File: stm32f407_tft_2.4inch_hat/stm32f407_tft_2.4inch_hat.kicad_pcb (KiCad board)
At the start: 2 copper layers, 62.5 x 71 mm, 3 parts, among them P1 Conn_02x25_Row_Letter_First_S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, P2 Conn_02x25_Row_Letter_First_S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, U1 CR2013-MI2120

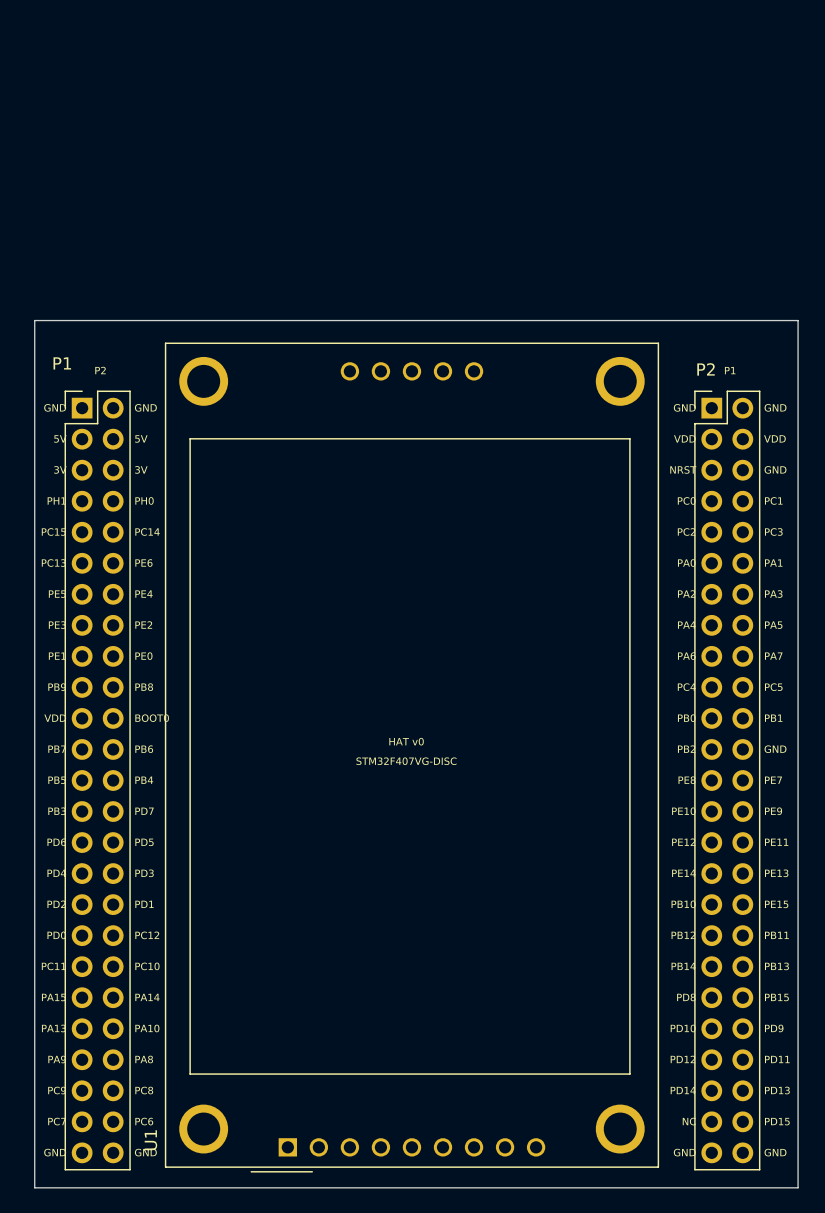
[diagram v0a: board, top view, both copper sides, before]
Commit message: Add 3 connector for i2c & uart
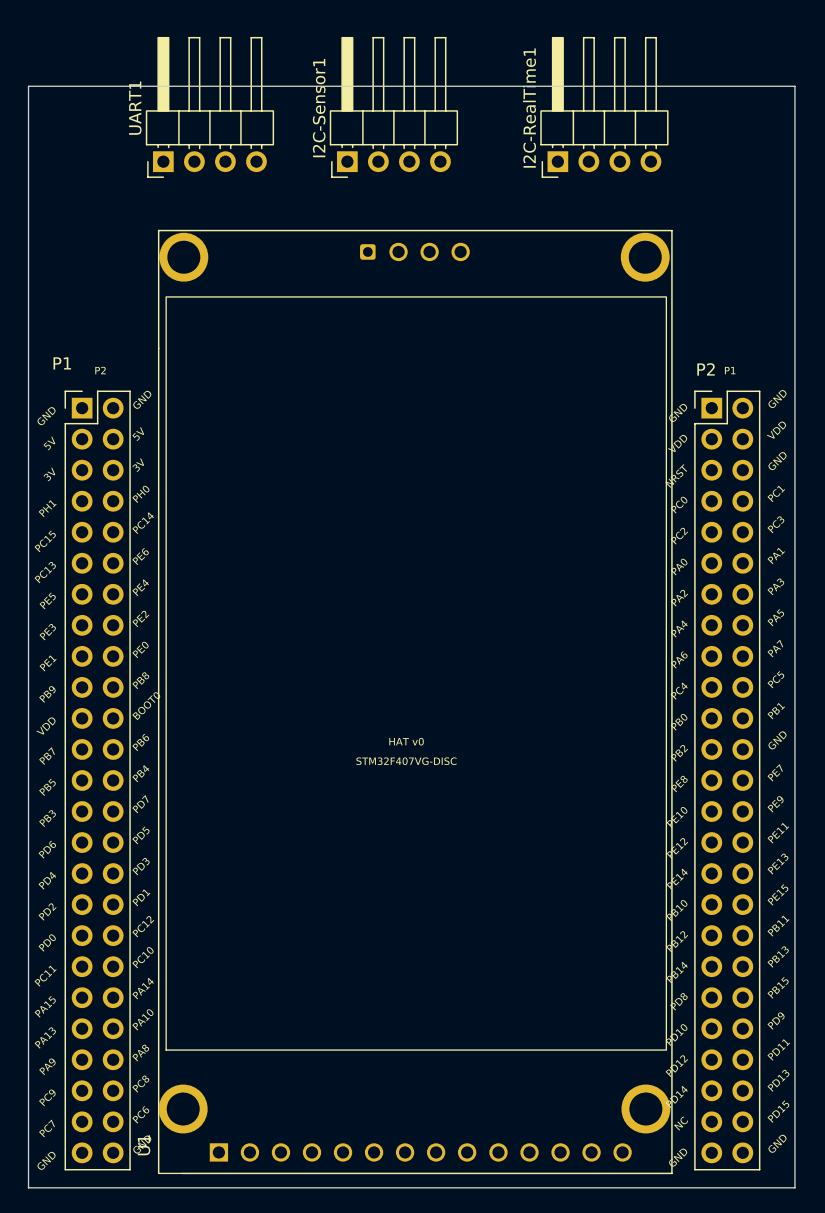
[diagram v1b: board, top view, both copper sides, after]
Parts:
- added I2C-RealTime1: Conn_01x04_Pin, Connector_PinHeader_2.54mm:PinHeader_1x04_P2.54mm_Horizontal, F.Cu at (160.2, 50.8)
- added I2C-Sensor1: Conn_01x04_Pin, Connector_PinHeader_2.54mm:PinHeader_1x04_P2.54mm_Horizontal, F.Cu at (142.9, 50.8)
- added UART1: Conn_01x04_Pin, Connector_PinHeader_2.54mm:PinHeader_1x04_P2.54mm_Horizontal, F.Cu at (127.9, 50.8)
- P1: value Conn_02x25_Row_Letter_First_Shielded -> STM32F407-DISC P1
- P2: value Conn_02x25_Row_Letter_First_Shielded -> STM32F407-DISC P2
- U1: value CR2013-MI2120 -> TFT SPI 240x320
- moved U1 0.70 mm to (137.5, 131.9)
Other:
- board size 62.5 x 71 mm -> 62.7 x 90.2 mm

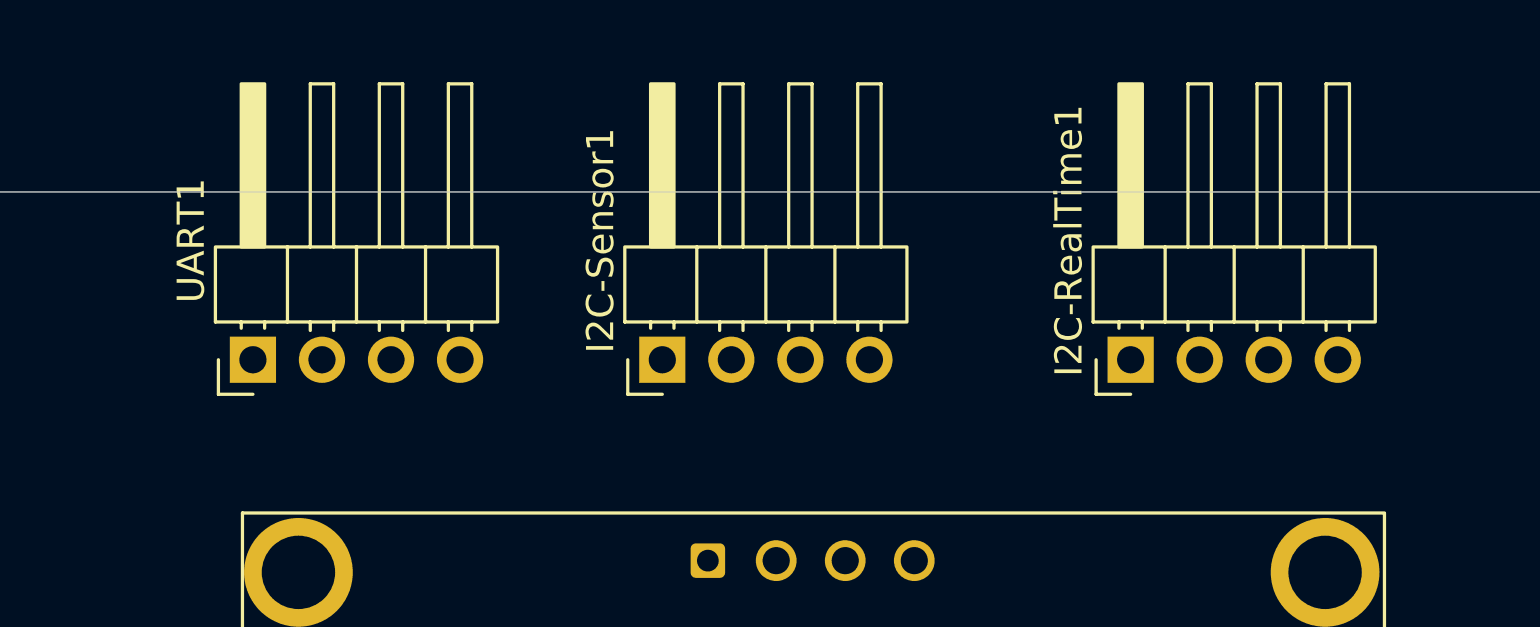
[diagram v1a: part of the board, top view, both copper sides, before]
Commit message: Update sch pin j1 & j2
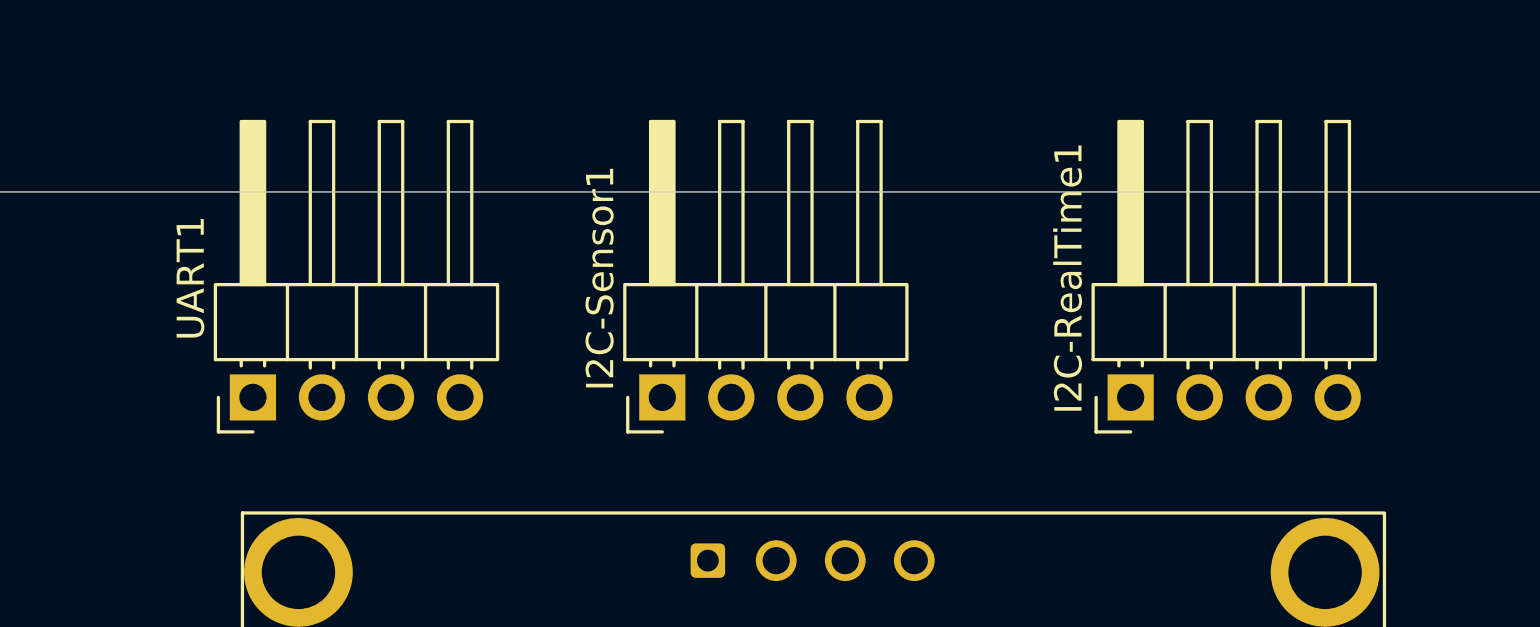
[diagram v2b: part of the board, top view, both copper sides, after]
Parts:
- moved I2C-RealTime1 1.38 mm to (160.2, 52.1)
- moved I2C-Sensor1 1.38 mm to (142.9, 52.1)
- moved UART1 1.38 mm to (127.9, 52.1)
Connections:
- I2C-RealTime1 pad 1: unconnected-(I2C-RealTime1-Pin_1-Pad1) -> /I2C_SDA
- I2C-RealTime1 pad 2: unconnected-(I2C-RealTime1-Pin_2-Pad2) -> /3V
- I2C-RealTime1 pad 3: unconnected-(I2C-RealTime1-Pin_3-Pad3) -> /GND
- I2C-RealTime1 pad 4: unconnected-(I2C-RealTime1-Pin_4-Pad4) -> /I2C_SCL
- I2C-Sensor1 pad 1: unconnected-(I2C-Sensor1-Pin_1-Pad1) -> /I2C_SDA
- I2C-Sensor1 pad 2: unconnected-(I2C-Sensor1-Pin_2-Pad2) -> /3V
- I2C-Sensor1 pad 3: unconnected-(I2C-Sensor1-Pin_3-Pad3) -> /GND
- I2C-Sensor1 pad 4: unconnected-(I2C-Sensor1-Pin_4-Pad4) -> /I2C_SCL
- P1 pad 1: (no net) -> /GND
- P1 pad 10: (no net) -> /PA9
- P1 pad 11: (no net) -> /PA14
- P1 pad 12: (no net) -> /PA13
- P1 pad 13: (no net) -> /PC10
- P1 pad 14: (no net) -> /PA15
- P1 pad 15: (no net) -> /PC12
- P1 pad 16: (no net) -> /PC11
- P1 pad 17: (no net) -> /PD1
- P1 pad 18: (no net) -> /PD0
- P1 pad 19: (no net) -> /PD3
- P1 pad 2: (no net) -> /GND
- P1 pad 20: (no net) -> /PD2
- P1 pad 21: (no net) -> /PD5
- P1 pad 22: (no net) -> /PD4
- P1 pad 23: (no net) -> /PD7
- P1 pad 24: (no net) -> /PD6
- P1 pad 25: (no net) -> /PB4
- P1 pad 26: (no net) -> /PB3
- P1 pad 27: (no net) -> /PB6
- P1 pad 28: (no net) -> /PB5
- P1 pad 29: (no net) -> /BOOT0
- P1 pad 3: (no net) -> /PC6
- P1 pad 30: (no net) -> /PB7
- P1 pad 31: (no net) -> /PB8
- P1 pad 32: (no net) -> /GND
- P1 pad 33: (no net) -> /PE0
- P1 pad 34: (no net) -> /PB9
- P1 pad 35: (no net) -> /PE2
- P1 pad 36: (no net) -> /PE1
- P1 pad 37: (no net) -> /PE4
- P1 pad 38: (no net) -> /PE3
- P1 pad 39: (no net) -> /PE6
- P1 pad 4: (no net) -> /GND
- P1 pad 40: (no net) -> /PE5
- P1 pad 41: (no net) -> /PC14
- P1 pad 42: (no net) -> /PC15
- P1 pad 43: (no net) -> /PH0
- P1 pad 44: (no net) -> /PH1
- P1 pad 45: (no net) -> /3V
- P1 pad 46: (no net) -> /3V
- P1 pad 47: (no net) -> /5V
- P1 pad 48: (no net) -> /5V
- P1 pad 49: (no net) -> /GND
- P1 pad 5: (no net) -> /PC8
- P1 pad 50: (no net) -> /GND
- P1 pad 6: (no net) -> /PC7
- P1 pad 7: (no net) -> /PA8
- P1 pad 8: (no net) -> /PC9
- P1 pad 9: (no net) -> /PA10
- P2 pad 1: (no net) -> /GND
- P2 pad 10: (no net) -> /PD9
- P2 pad 11: (no net) -> /PD8
- P2 pad 12: (no net) -> /PB15
- P2 pad 13: (no net) -> /PB14
- P2 pad 14: (no net) -> /PB13
- P2 pad 15: (no net) -> /PB12
- P2 pad 16: (no net) -> unconnected-(P2-PA5-Pad16)
- P2 pad 17: (no net) -> /PB10
- P2 pad 18: (no net) -> /PE15
- P2 pad 19: (no net) -> /PE14
- P2 pad 2: (no net) -> /GND
- P2 pad 20: (no net) -> /PE13
- P2 pad 21: (no net) -> /PE12
- P2 pad 22: (no net) -> /PE11
- P2 pad 23: (no net) -> /PE10
- P2 pad 24: (no net) -> /PE9
- P2 pad 25: (no net) -> /PE8
- P2 pad 26: (no net) -> /PE7
- P2 pad 27: (no net) -> /PB2
- P2 pad 28: (no net) -> /GND
- P2 pad 29: (no net) -> /PB0
- P2 pad 3: (no net) -> /NC
- P2 pad 30: (no net) -> /PB1
- P2 pad 31: (no net) -> /PC4
- P2 pad 32: (no net) -> /PC5
- P2 pad 33: (no net) -> /PA6
- P2 pad 34: (no net) -> /PA7
- P2 pad 35: (no net) -> /PA4
- P2 pad 36: (no net) -> /PA5
- P2 pad 37: (no net) -> unconnected-(P2-PB14-Pad37)
- P2 pad 38: (no net) -> /PA3
- P2 pad 39: (no net) -> /PA0
- P2 pad 4: (no net) -> /PD15
- P2 pad 40: (no net) -> /PA1
- P2 pad 41: (no net) -> /GND
- P2 pad 42: (no net) -> /PC3
- P2 pad 43: (no net) -> /GND
- P2 pad 44: (no net) -> /PC1
- P2 pad 45: (no net) -> /GND
- P2 pad 46: (no net) -> /GND
- P2 pad 47: (no net) -> /GND
- P2 pad 48: (no net) -> /GND
- P2 pad 49: (no net) -> /GND
- P2 pad 5: (no net) -> /PD14
- P2 pad 50: (no net) -> /GND
- P2 pad 6: (no net) -> /PD13
- P2 pad 7: (no net) -> /PD12
- P2 pad 8: (no net) -> /PD11
- P2 pad 9: (no net) -> /PD10
- UART1 pad 1: unconnected-(UART1-Pin_1-Pad1) -> /3V
- UART1 pad 2: unconnected-(UART1-Pin_2-Pad2) -> /UART_RX
- UART1 pad 3: unconnected-(UART1-Pin_3-Pad3) -> /UART_TX
- UART1 pad 4: unconnected-(UART1-Pin_4-Pad4) -> /GND

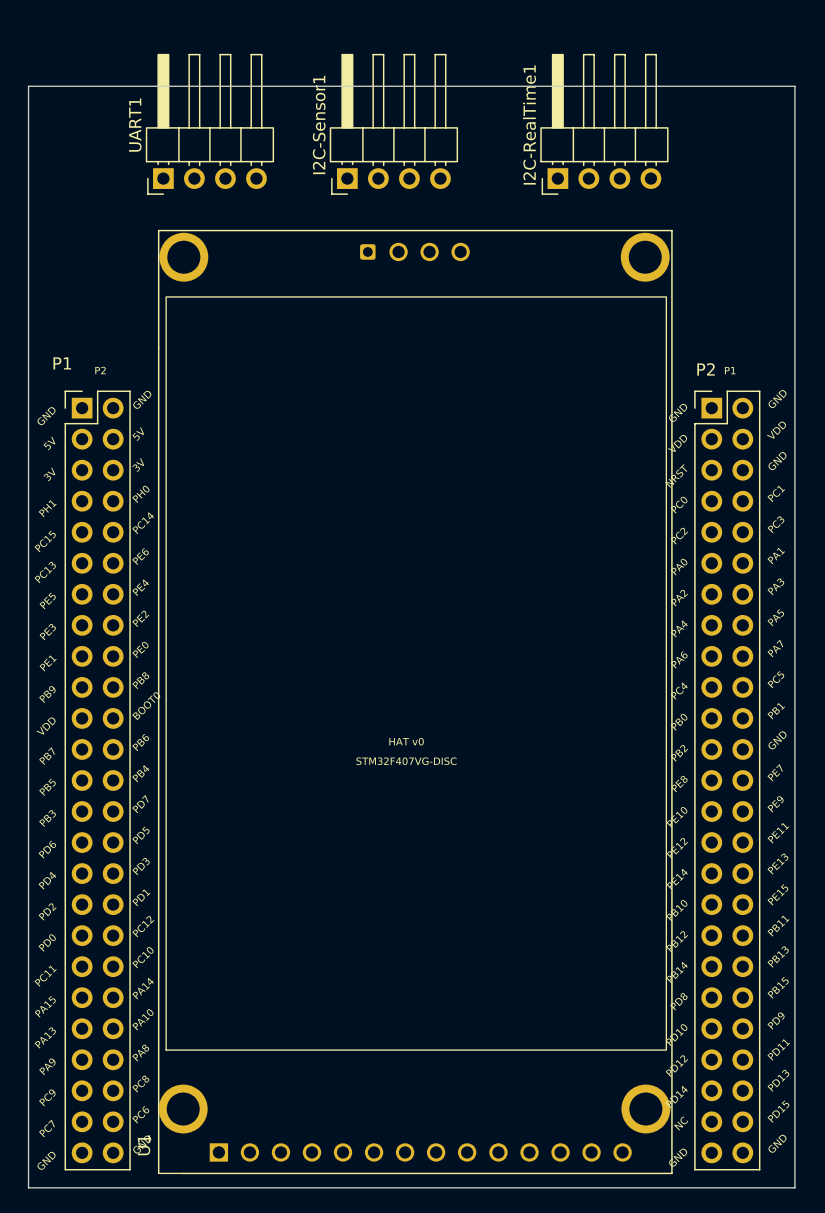
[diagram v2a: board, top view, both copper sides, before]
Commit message: Fix pinout pcb & sch are not correct
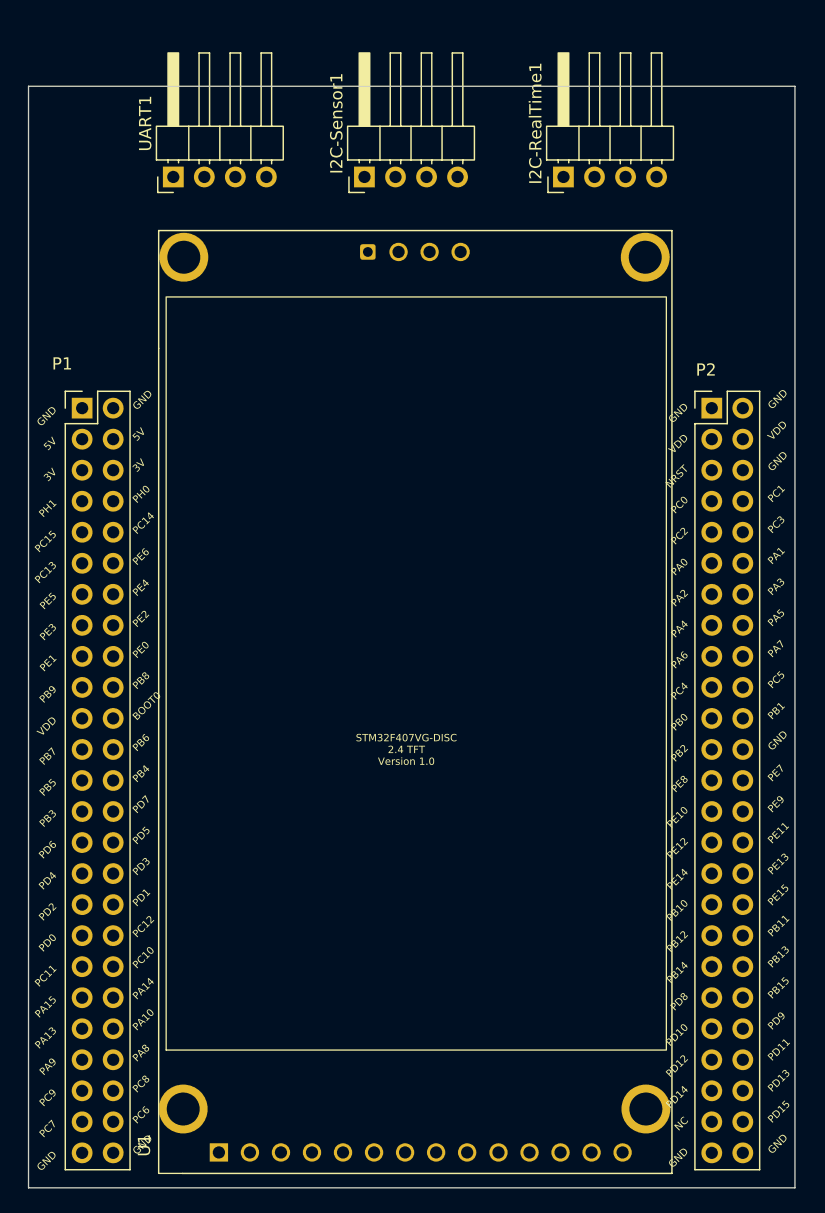
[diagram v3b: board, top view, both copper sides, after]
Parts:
- moved I2C-Sensor1 1.41 mm to (144.3, 52.0)
- moved UART1 0.82 mm to (128.7, 52.0)
- moved I2C-RealTime1 0.48 mm to (160.6, 52.0)
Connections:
- I2C-RealTime1 pad 1: /I2C_SDA -> /I2C2_SCL
- I2C-RealTime1 pad 2: /3V -> /I2C2_SDA
- I2C-RealTime1 pad 3: /GND -> /3V
- I2C-RealTime1 pad 4: /I2C_SCL -> /GND
- I2C-Sensor1 pad 1: /I2C_SDA -> /I2C2_SCL
- I2C-Sensor1 pad 2: /3V -> /I2C2_SDA
- I2C-Sensor1 pad 3: /GND -> /3V
- I2C-Sensor1 pad 4: /I2C_SCL -> /GND
- P1 pad 10: /PA9 -> /PC14
- P1 pad 11: /PA14 -> /LCD_T_IRQ
- P1 pad 12: /PA13 -> /PE6
- P1 pad 13: /PC10 -> /LCD_T_CS
- P1 pad 14: /PA15 -> /LCD_SD_CS
- P1 pad 15: /PC12 -> /PE1
- P1 pad 16: /PC11 -> /PE2
- P1 pad 17: /PD1 -> /LCD_CS
- P1 pad 18: /PD0 -> /PE0
- P1 pad 19: /PD3 -> /VDD
- P1 pad 20: /PD2 -> /PB8
- P1 pad 21: /PD5 -> /PB7
- P1 pad 22: /PD4 -> /BOOT0
- P1 pad 23: /PD7 -> /PB5
- P1 pad 24: /PD6 -> /PB6
- P1 pad 25: /PB4 -> /PB3
- P1 pad 26: /PB3 -> /PB4
- P1 pad 27: /PB6 -> /PD6
- P1 pad 28: /PB5 -> /PD7
- P1 pad 29: /BOOT0 -> /PD4
- P1 pad 3: /PC6 -> /5V
- P1 pad 30: /PB7 -> /PD5
- P1 pad 31: /PB8 -> /PD2
- P1 pad 32: /GND -> /PD3
- P1 pad 33: /PE0 -> /PD0
- P1 pad 34: /PB9 -> /PD1
- P1 pad 35: /PE2 -> /LCD_SD_MISO
- P1 pad 36: /PE1 -> /LCD_SD_MOSI
- P1 pad 37: /PE4 -> /PA15
- P1 pad 38: /PE3 -> /LCD_SD_CLK
- P1 pad 39: /PE6 -> /PA13
- P1 pad 4: /GND -> /5V
- P1 pad 40: /PE5 -> /PA14
- P1 pad 41: /PC14 -> /PA9
- P1 pad 42: /PC15 -> /PA10
- P1 pad 43: /PH0 -> /PC9
- P1 pad 44: /PH1 -> /PA8
- P1 pad 45: /3V -> /PC7
- P1 pad 46: /3V -> /PC8
- P1 pad 47: /5V -> /GND
- P1 pad 48: /5V -> /PC6
- P1 pad 5: /PC8 -> /3V
- P1 pad 6: /PC7 -> /3V
- P1 pad 7: /PA8 -> /PH1
- P1 pad 8: /PC9 -> /PH0
- P1 pad 9: /PA10 -> /PC15
- P2 pad 10: /PD9 -> /PC3
- P2 pad 11: /PD8 -> /PA0
- P2 pad 12: /PB15 -> /PA1
- P2 pad 13: /PB14 -> /DBG_UART2_RX
- P2 pad 14: /PB13 -> /DBG_UART2_TX
- P2 pad 15: /PB12 -> /PA4
- P2 pad 16: unconnected-(P2-PA5-Pad16) -> /PA5
- P2 pad 17: /PB10 -> /PA6
- P2 pad 18: /PE15 -> /PA7
- P2 pad 19: /PE14 -> /PC4
- P2 pad 20: /PE13 -> /PC5
- P2 pad 21: /PE12 -> /PB0
- P2 pad 22: /PE11 -> /PB1
- P2 pad 23: /PE10 -> /PB2
- P2 pad 24: /PE9 -> /GND
- P2 pad 27: /PB2 -> /PE10
- P2 pad 28: /GND -> /PE9
- P2 pad 29: /PB0 -> /PE12
- P2 pad 3: /NC -> /VDD
- P2 pad 30: /PB1 -> /PE11
- P2 pad 31: /PC4 -> /PE14
- P2 pad 32: /PC5 -> /PE13
- P2 pad 33: /PA6 -> /I2C2_SCL
- P2 pad 34: /PA7 -> /PE15
- P2 pad 35: /PA4 -> /PB12
- P2 pad 36: /PA5 -> /I2C2_SDA
- P2 pad 37: unconnected-(P2-PB14-Pad37) -> /PB14
- P2 pad 38: /PA3 -> /LCD_SCK
- P2 pad 39: /PA0 -> /PD8
- P2 pad 4: /PD15 -> /VDD
- P2 pad 40: /PA1 -> /LCD_MOSI
- P2 pad 41: /GND -> /LCD_RESET
- P2 pad 42: /PC3 -> /LCD_DC
- P2 pad 43: /GND -> /PD12
- P2 pad 44: /PC1 -> /PD11
- P2 pad 45: /GND -> /PD14
- P2 pad 46: /GND -> /PD13
- P2 pad 47: /GND -> /NC
- P2 pad 48: /GND -> /PD15
- P2 pad 5: /PD14 -> /NRST
- P2 pad 6: /PD13 -> /GND
- P2 pad 7: /PD12 -> /PC0
- P2 pad 8: /PD11 -> /PC1
- P2 pad 9: /PD10 -> /LCD_MISO
- U1 pad 1: unconnected-(U1-VCC-Pad1) -> /5V
- U1 pad 10: unconnected-(U1-T_CLK-Pad10) -> /LCD_T_CLK
- U1 pad 11: unconnected-(U1-T_CS-Pad11) -> /LCD_T_CS
- U1 pad 12: unconnected-(U1-T_MOSI-Pad12) -> /LCD_T_MOSI
- U1 pad 13: unconnected-(U1-T_MISO-Pad13) -> /LCD_T_MISO
- U1 pad 14: unconnected-(U1-T_IRQ-Pad14) -> /LCD_T_IRQ
- U1 pad 15: unconnected-(U1-SD_CLK-Pad15) -> /LCD_SD_CLK
- U1 pad 16: unconnected-(U1-SD_MISO-Pad16) -> /LCD_SD_MISO
- U1 pad 17: unconnected-(U1-SD_MOSI-Pad17) -> /LCD_SD_MOSI
- U1 pad 18: unconnected-(U1-SD_CS-Pad18) -> /LCD_SD_CS
- U1 pad 2: unconnected-(U1-GND-Pad2) -> /GND
- U1 pad 3: unconnected-(U1-~{CS}-Pad3) -> /LCD_CS
- U1 pad 4: unconnected-(U1-RESET-Pad4) -> /LCD_RESET
- U1 pad 5: unconnected-(U1-D/~{C}-Pad5) -> /LCD_DC
- U1 pad 6: unconnected-(U1-MOSI-Pad6) -> /LCD_MOSI
- U1 pad 7: unconnected-(U1-SCK-Pad7) -> /LCD_SCK
- U1 pad 8: unconnected-(U1-LED-Pad8) -> /5V
- U1 pad 9: unconnected-(U1-MISO-Pad9) -> /LCD_MISO
- UART1 pad 2: /UART_RX -> /DBG_UART2_RX
- UART1 pad 3: /UART_TX -> /DBG_UART2_TX
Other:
- board text added: "STM32F407VG-DISC 2.4 TFT Version 1.0"
- board text removed: "HAT v0"
- board text removed: "P1"
- board text removed: "P2"
- board text removed: "STM32F407VG-DISC"
